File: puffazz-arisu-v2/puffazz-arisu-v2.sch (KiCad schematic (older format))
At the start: 185 parts, among them SW1 SW_Push, U1 ATmega32U4-AU, Y1 16MHz

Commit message: Finished scematic
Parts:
- removed D1: D_Schottky, symbol Device:D_Schottky
- added MX_#BKSP2: MX-NoLED, Button_Switch_Keyboard:SW_Cherry_MX_2.00u_PCB, symbol MX_Alps_Hybrid:MX-NoLED
- C1, C2, C3, C4, C5: footprint (none) -> Capacitor_SMD:C_0805_2012Metric
- C10, C11, C12, C13, C14, C15, C16, C17, C18, C19, C20, C21, C6, C7, C8, C9: renamed from C?; footprint (none) -> Capacitor_SMD:C_0805_2012Metric
- D10, D11, D12, D13, D14, D15, D16, D17, D18, D19, D2, D20, D21, D22, D23, D24, D25, D26, D27, D28, D29, D3, D30, D31, D32, D33, D34, D35, D36, D37, D38, D39, D4, D40, D41, D42, D43, D44, D45, D46, D47, D48, D49, D5, D50, D51, D52, D53, D54, D55, D56, D57, D58, D59, D6, D60, D61, D62, D63, D64, D65, D66, D67, D68, D7, D8, D9: renamed from D?; footprint (none) -> Diode_SMD:D_SOD-123
- F1: footprint (none) -> Fuse:Fuse_1206_3216Metric
- MX_"1, MX_#+1, MX_#-1, MX_#0, MX_#1, MX_#2, MX_#3, MX_#4, MX_#5, MX_#6, MX_#7, MX_#8, MX_#9, MX_#PGUP1, MX_#`1, MX_#|1, MX_:1, MX_<1, MX_>1, MX_?1, MX_A1, MX_B1, MX_C1, MX_D1, MX_DOWN1, MX_E1, MX_ESC1, MX_F1, MX_FN1, MX_G1, MX_H1, MX_I1, MX_J1, MX_K1, MX_L1, MX_LEFT1, MX_LWIN1, MX_M1, MX_N1, MX_O1, MX_P1, MX_PGDN1, MX_Q1, MX_R1, MX_RIGHT1, MX_S1, MX_T1, MX_U1, MX_UP1, MX_V1, MX_W1, MX_X1, MX_Y1, MX_Z1, MX_[1, MX_]1: footprint (none) -> Button_Switch_Keyboard:SW_Cherry_MX_1.00u_PCB
- MX_#TAB1, MX_LALT2, MX_LCTRL1, MX_RALT1: footprint (none) -> Button_Switch_Keyboard:SW_Cherry_MX_1.50u_PCB
- MX_BCKSP1, MX_SPACE1: footprint (none) -> Button_Switch_Keyboard:SW_Cherry_MX_2.00u_PCB
- MX_CAPS1, MX_CAPS2, MX_RSHIFT1: footprint (none) -> Button_Switch_Keyboard:SW_Cherry_MX_1.75u_PCB
- MX_LALT1: footprint (none) -> Button_Switch_Keyboard:SW_Cherry_MX_1.25u_PCB
- MX_LSHIFT1, MX_RETURN1, MX_SPACE2: footprint (none) -> Button_Switch_Keyboard:SW_Cherry_MX_2.25u_PCB
- MX_SPACE3: footprint (none) -> Button_Switch_Keyboard:SW_Cherry_MX_2.75u_PCB
- R1, R2, R3, R4, R5, R6: footprint (none) -> Resistor_SMD:R_0805_2012Metric
- SW1: footprint (none) -> Button_Switch_SMD:SW_SPST_SKQG_WithStem
- USB1: renamed from USB?; footprint (none) -> Connector_USB:USB_C_Receptacle_HRO_TYPE-C-31-M-12
- Y1: footprint (none) -> Crystal:Crystal_SMD_3225-4Pin_3.2x2.5mm
- gave numbers to parts that had none: 14
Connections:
- net labels added: ROW0, ROW1, ROW2, ROW3, ROW4, ROW5, ROW6, ROW7, ROW8, ROW9
- wire segments 251 -> 355
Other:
- moved on the sheet: D10, D11, D12, D13, D14, D15, D16, D17, D25, D26, D27, D28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

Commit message: Finished placing switch footprints on to the pcb
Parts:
- MX_BCKSP1: footprint Button_Switch_Keyboard:SW_Cherry_MX_2.00u_PCB -> Button_Switch_Keyboard:SW_Cherry_MX_1.50u_PCB
- MX_CAPS2: footprint Button_Switch_Keyboard:SW_Cherry_MX_1.75u_PCB -> Button_Switch_Keyboard:SW_Cherry_MX_1.00u_PCB
- U1: symbol MCU_Microchip_ATmega:ATmega32U4-AU -> puffazz-arisu-v2-rescue:ATmega32U4-AU-MCU_Microchip_ATmega
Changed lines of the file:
@@
 EESchema Schematic File Version 4
+LIBS:puffazz-arisu-v2-cache
 EELAYER 30 0
 EELAYER END
@@
 F 0 "MX_BCKSP1" H 13083 3223 60  0000 C CNN
 F 1 "MX-NoLED" H 13083 3149 20  0000 C CNN
-F 2 "Button_Switch_Keyboard:SW_Cherry_MX_2.00u_PCB" H 12425 2975 60  0001 C CNN
+F 2 "Button_Switch_Keyboard:SW_Cherry_MX_1.50u_PCB" H 12425 2975 60  0001 C CNN
 F 3 "" H 12425 2975 60  0001 C CNN
 	1    13050 3000
@@
 F 0 "MX_CAPS2" H 6033 4023 60  0000 C CNN
 F 1 "MX-NoLED" H 6033 3949 20  0000 C CNN
-F 2 "Button_Switch_Keyboard:SW_Cherry_MX_1.75u_PCB" H 5375 3775 60  0001 C CNN
+F 2 "Button_Switch_Keyboard:SW_Cherry_MX_1.00u_PCB" H 5375 3775 60  0001 C CNN
 F 3 "" H 5375 3775 60  0001 C CNN
 	1    6000 3800
@@
 	2900 4650 3350 4650
 $Comp
-L MCU_Microchip_ATmega:ATmega32U4-AU U1
+L puffazz-arisu-v2-rescue:ATmega32U4-AU-MCU_Microchip_ATmega U1
 U 1 1 5F269BC8
 P 2900 2850

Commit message: Fixed usb-c footprint not working with rats nest view
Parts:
- USB1: footprint Connector_USB:USB_C_Receptacle_HRO_TYPE-C-31-M-12 -> Type-C:HRO-TYPE-C-31-M-12-Assembly
- Y1: footprint Crystal:Crystal_SMD_3225-4Pin_3.2x2.5mm -> Type-C:HRO-TYPE-C-31-M-12-HandSoldering
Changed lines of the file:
@@
 F 0 "Y1" V 1854 1794 50  0000 L CNN
 F 1 "16MHz" V 1945 1794 50  0000 L CNN
-F 2 "Crystal:Crystal_SMD_3225-4Pin_3.2x2.5mm" H 1900 1650 50  0001 C CNN
+F 2 "Type-C:HRO-TYPE-C-31-M-12-HandSoldering" H 1900 1650 50  0001 C CNN
 F 3 "~" H 1900 1650 50  0001 C CNN
 	1    1900 1650
@@
 F 0 "USB1" H 1283 10447 60  0000 C CNN
 F 1 "HRO-TYPE-C-31-M-12" H 1283 10341 60  0000 C CNN
-F 2 "Connector_USB:USB_C_Receptacle_HRO_TYPE-C-31-M-12" H 1450 9650 60  0001 C CNN
+F 2 "Type-C:HRO-TYPE-C-31-M-12-Assembly" H 1450 9650 60  0001 C CNN
 F 3 "" H 1450 9650 60  0001 C CNN
 	1    1450 9650

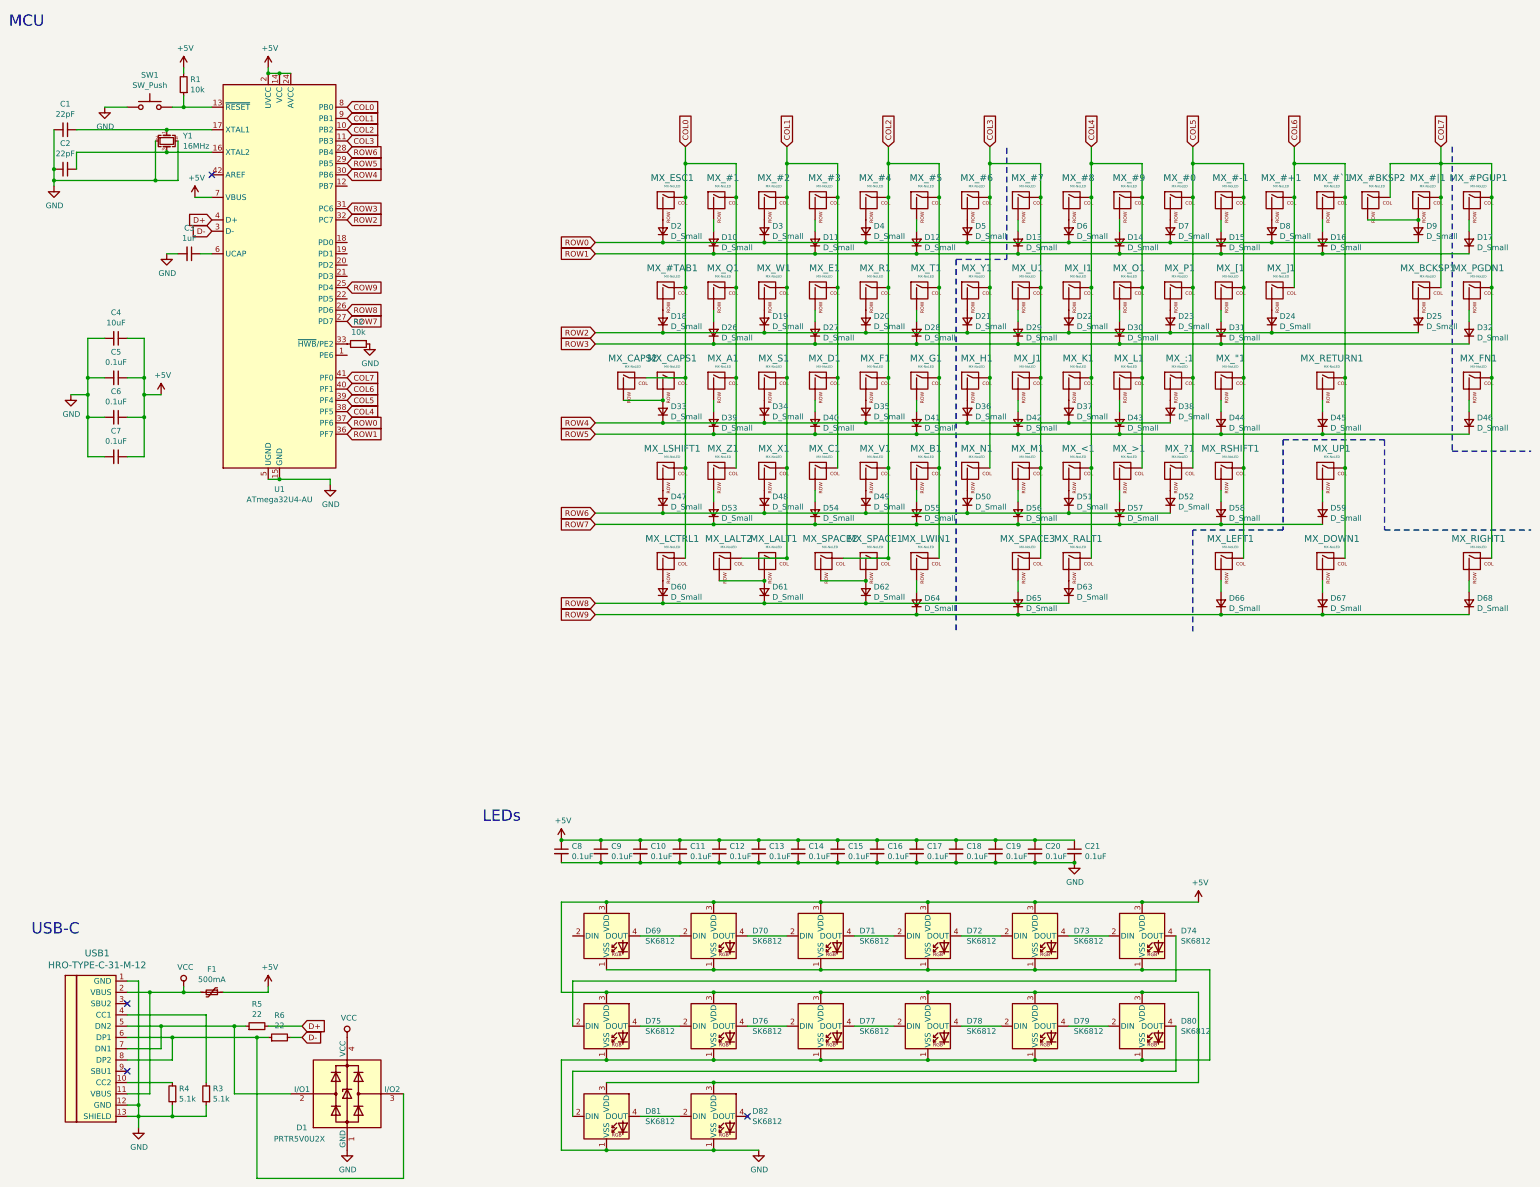
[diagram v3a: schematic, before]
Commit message: Finished routing switches and RGB LED
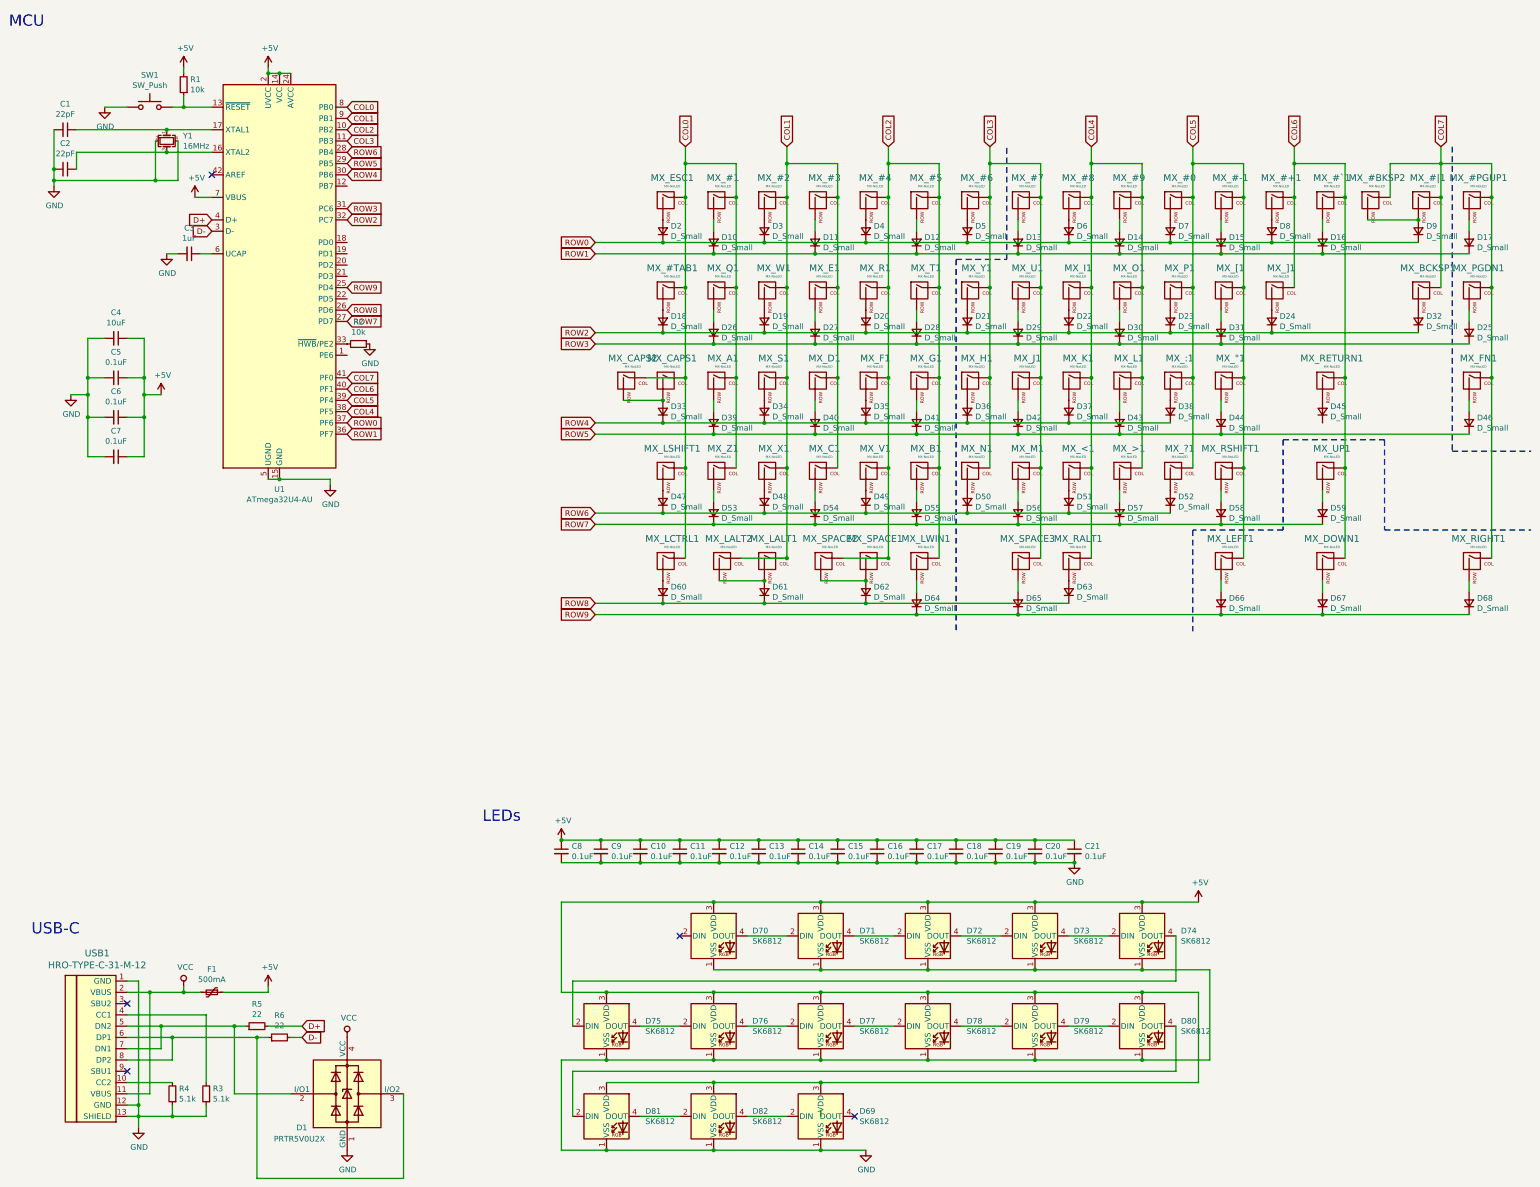
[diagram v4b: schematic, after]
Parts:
- Y1: footprint Type-C:HRO-TYPE-C-31-M-12-HandSoldering -> Crystal:Crystal_SMD_3225-4Pin_3.2x2.5mm_HandSoldering
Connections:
- net ROW2: now also D32.1 (K); no longer D25.1 (K)
- net ROW3: now also D25.1 (K); no longer D32.1 (K)
- net ROW5: no longer D45.1 (K)
- net at MX_BCKSP1.2 (ROW): now also D32.2 (A); no longer D25.2 (A)
- net at D69.2 (DIN): now also D82.4 (DOUT)
- net at D69.4 (DOUT): no longer D70.2 (DIN)
- net at MX_PGDN1.2 (ROW): now also D25.2 (A); no longer D32.2 (A)
- no-connect marks 4 -> 5
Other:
- moved on the sheet: D25, D32, D45, D69
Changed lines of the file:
@@
 F 0 "Y1" V 1854 1794 50  0000 L CNN
 F 1 "16MHz" V 1945 1794 50  0000 L CNN
-F 2 "Type-C:HRO-TYPE-C-31-M-12-HandSoldering" H 1900 1650 50  0001 C CNN
+F 2 "Crystal:Crystal_SMD_3225-4Pin_3.2x2.5mm_HandSoldering" H 1900 1650 50  0001 C CNN
 F 3 "~" H 1900 1650 50  0001 C CNN
 	1    1900 1650
@@
 $EndComp
 $Comp
-L Device:C_Small C4
-U 1 1 5F28E489
-P 1450 3400
-F 0 "C4" V 1221 3400 50  0000 C CNN
-F 1 "10uF" V 1312 3400 50  0000 C CNN
-F 2 "Capacitor_SMD:C_0805_2012Metric" H 1450 3400 50  0001 C CNN
-F 3 "~" H 1450 3400 50  0001 C CNN
-	1    1450 3400
-	0    1    1    0
-$EndComp
-$Comp
-L Device:C_Small C5
-U 1 1 5F28EF4D
-P 1450 3750
-F 0 "C5" V 1221 3750 50  0000 C CNN
-F 1 "0.1uF" V 1312 3750 50  0000 C CNN
-F 2 "Capacitor_SMD:C_0805_2012Metric" H 1450 3750 50  0001 C CNN
-F 3 "~" H 1450 3750 50  0001 C CNN
-	1    1450 3750
-	0    1    1    0
-$EndComp
-$Comp
-L Device:C_Small C6
-U 1 1 5F28F33C
-P 1450 4100
-F 0 "C6" V 1221 4100 50  0000 C CNN
-F 1 "0.1uF" V 1312 4100 50  0000 C CNN
-F 2 "Capacitor_SMD:C_0805_2012Metric" H 1450 4100 50  0001 C CNN
-F 3 "~" H 1450 4100 50  0001 C CNN
-	1    1450 4100
-	0    1    1    0
-$EndComp
-$Comp
-L Device:C_Small C7
-U 1 1 5F28F941
-P 1450 4450
-F 0 "C7" V 1221 4450 50  0000 C CNN
-F 1 "0.1uF" V 1312 4450 50  0000 C CNN
-F 2 "Capacitor_SMD:C_0805_2012Metric" H 1450 4450 50  0001 C CNN
-F 3 "~" H 1450 4450 50  0001 C CNN
-	1    1450 4450
-	0    1    1    0
-$EndComp
-Wire Wire Line
-	1350 3400 1200 3400
-Wire Wire Line
-	1200 3400 1200 3750
-Wire Wire Line
-	1200 4450 1350 4450
-Wire Wire Line
-	1350 4100 1200 4100
-Connection ~ 1200 4100
-Wire Wire Line
-	1200 4100 1200 4450
-Wire Wire Line
-	1350 3750 1200 3750
-Connection ~ 1200 3750
-Wire Wire Line
-	1200 3750 1200 3900
-Wire Wire Line
-	1550 3400 1700 3400
-Wire Wire Line
-	1700 4450 1550 4450
-Wire Wire Line
-	1550 4100 1700 4100
-Connection ~ 1700 4100
-Wire Wire Line
-	1700 4100 1700 4450
-Wire Wire Line
-	1550 3750 1700 3750
-Connection ~ 1700 3750
-Wire Wire Line
-	1700 3750 1700 3900
-Wire Wire Line
-	1700 3900 1850 3900
-Connection ~ 1700 3900
-Wire Wire Line
-	1700 3900 1700 4100
-$Comp
-L power:+5V #PWR0107
-U 1 1 5F296773
-P 1850 3900
-F 0 "#PWR0107" H 1850 3750 50  0001 C CNN
-F 1 "+5V" H 1865 4073 50  0000 C CNN
-F 2 "" H 1850 3900 50  0001 C CNN
-F 3 "" H 1850 3900 50  0001 C CNN
-	1    1850 3900
-	1    0    0    -1
-$EndComp
-$Comp
-L power:GND #PWR0108
-U 1 1 5F296B96
-P 1050 3900
-F 0 "#PWR0108" H 1050 3650 50  0001 C CNN
-F 1 "GND" H 1055 3727 50  0000 C CNN
-F 2 "" H 1050 3900 50  0001 C CNN
-F 3 "" H 1050 3900 50  0001 C CNN
-	1    1050 3900
-	1    0    0    -1
-$EndComp
-Wire Wire Line
-	1050 3900 1200 3900
-Connection ~ 1200 3900
-Wire Wire Line
-	1200 3900 1200 4100
-$Comp
 L Device:R_Small R2
 U 1 1 5F29845C
@@
 L LED:SK6812 D69
 U 1 1 5F3782C0
-P 5800 8700
-F 0 "D69" H 6144 8746 50  0000 L CNN
-F 1 "SK6812" H 6144 8655 50  0000 L CNN
-F 2 "LED_SMD:LED_SK6812_PLCC4_5.0x5.0mm_P3.2mm" H 5850 8400 50  0001 L TNN
-F 3 "https://cdn-shop.adafruit.com/product-files/1138/SK6812+LED+datasheet+.pdf" H 5900 8325 50  0001 L TNN
-	1    5800 8700
+P 7700 10300
+F 0 "D69" H 8044 10346 50  0000 L CNN
+F 1 "SK6812" H 8044 10255 50  0000 L CNN
+F 2 "LED_SMD:LED_SK6812_PLCC4_5.0x5.0mm_P3.2mm" H 7750 10000 50  0001 L TNN
+F 3 "https://cdn-shop.adafruit.com/product-files/1138/SK6812+LED+datasheet+.pdf" H 7800 9925 50  0001 L TNN
+	1    7700 10300
 	1    0    0    -1
 $EndComp
@@
 $EndComp
 Wire Wire Line
-	6100 8700 6450 8700
-Wire Wire Line
 	7050 8700 7400 8700
 Wire Wire Line
@@
 Wire Wire Line
 	6100 10300 6450 10300
-NoConn ~ 7050 10300
 $Comp
 L power:+5V #PWR0115
@@
 	11050 8400 10550 8400
 Connection ~ 6750 8400
-Wire Wire Line
-	6750 8400 5800 8400
 Connection ~ 7700 8400
 Wire Wire Line
@@
 	10550 8400 9600 8400
 Wire Wire Line
-	5800 8400 5400 8400
-Wire Wire Line
 	5400 8400 5400 9200
 Wire Wire Line
 	5400 9200 5800 9200
-Connection ~ 5800 8400
 Connection ~ 5800 9200
 Wire Wire Line
@@
 	11050 9200 11050 10000
 Wire Wire Line
-	11050 10000 6750 10000
+	11050 10000 7700 10000
 Connection ~ 10550 9200
 Connection ~ 6750 10000
@@
 	6750 10000 5800 10000
 Wire Wire Line
-	5800 9000 6750 9000
-Wire Wire Line
 	11150 9000 11150 9800
 Wire Wire Line
 	11150 9800 10550 9800
-Connection ~ 6750 9000
 Wire Wire Line
 	6750 9000 7700 9000
@@
 L power:GND #PWR0116
 U 1 1 5F400838
-P 7150 10600
-F 0 "#PWR0116" H 7150 10350 50  0001 C CNN
-F 1 "GND" H 7155 10427 50  0000 C CNN
-F 2 "" H 7150 10600 50  0001 C CNN
-F 3 "" H 7150 10600 50  0001 C CNN
-	1    7150 10600
+P 8100 10600
+F 0 "#PWR0116" H 8100 10350 50  0001 C CNN
+F 1 "GND" H 8105 10427 50  0000 C CNN
+F 2 "" H 8100 10600 50  0001 C CNN
+F 3 "" H 8100 10600 50  0001 C CNN
+	1    8100 10600
 	1    0    0    -1
 $EndComp
-Wire Wire Line
-	7150 10600 6750 10600
 Connection ~ 6750 10600
 Text Notes 4700 7700 0    100  ~ 0
@@
 L Device:D_Small D25
 U 1 1 5F3E1B60
-P 13000 3250
-F 0 "D25" V 13046 3180 50  0000 R CNN
-F 1 "D_Small" V 12955 3180 50  0000 R CNN
-F 2 "Diode_SMD:D_SOD-123" V 13000 3250 50  0001 C CNN
-F 3 "~" V 13000 3250 50  0001 C CNN
-	1    13000 3250
+P 13450 3350
+F 0 "D25" V 13496 3280 50  0000 R CNN
+F 1 "D_Small" V 13405 3280 50  0000 R CNN
+F 2 "Diode_SMD:D_SOD-123" V 13450 3350 50  0001 C CNN
+F 3 "~" V 13450 3350 50  0001 C CNN
+	1    13450 3350
 	0    -1   -1   0
 $EndComp
@@
 L Device:D_Small D32
 U 1 1 5F4270C8
-P 13450 3350
-F 0 "D32" V 13496 3280 50  0000 R CNN
-F 1 "D_Small" V 13405 3280 50  0000 R CNN
-F 2 "Diode_SMD:D_SOD-123" V 13450 3350 50  0001 C CNN
-F 3 "~" V 13450 3350 50  0001 C CNN
-	1    13450 3350
+P 13000 3250
+F 0 "D32" V 13046 3180 50  0000 R CNN
+F 1 "D_Small" V 12955 3180 50  0000 R CNN
+F 2 "Diode_SMD:D_SOD-123" V 13000 3250 50  0001 C CNN
+F 3 "~" V 13000 3250 50  0001 C CNN
+	1    13000 3250
 	0    -1   -1   0
 $EndComp
@@
 L Device:D_Small D45
 U 1 1 5F4541F9
-P 12150 4150
-F 0 "D45" V 12196 4080 50  0000 R CNN
-F 1 "D_Small" V 12105 4080 50  0000 R CNN
-F 2 "Diode_SMD:D_SOD-123" V 12150 4150 50  0001 C CNN
-F 3 "~" V 12150 4150 50  0001 C CNN
-	1    12150 4150
+P 12150 4050
+F 0 "D45" V 12196 3980 50  0000 R CNN
+F 1 "D_Small" V 12105 3980 50  0000 R CNN
+F 2 "Diode_SMD:D_SOD-123" V 12150 4050 50  0001 C CNN
+F 3 "~" V 12150 4050 50  0001 C CNN
+	1    12150 4050
 	0    -1   -1   0
 $EndComp
@@
 	11250 4050 11250 3950
 Wire Wire Line
-	12150 4050 12150 3950
-Wire Wire Line
 	13450 4050 13450 3950
 Wire Wire Line
@@
 	10350 4250 11250 4250
 Connection ~ 11250 4250
-Wire Wire Line
-	11250 4250 12150 4250
 Text GLabel 5700 4150 0    50   Input ~ 0
 ROW4
@@
 Connection ~ 11250 3450
 Wire Wire Line
-	12150 4250 13450 4250
-Connection ~ 12150 4250
-Wire Wire Line
 	12150 5850 13450 5850
 Connection ~ 12150 5850
@@
 Wire Wire Line
 	2800 1050 2900 1050
-Wire Wire Line
-	1700 3400 1700 3750
 Connection ~ 2900 4650
 Wire Wire Line
@@
 	12550 2350 13000 2350
 Connection ~ 13000 2350
+Wire Wire Line
+	1700 3400 1700 3750
+Wire Wire Line
+	1200 3900 1200 4100
+Connection ~ 1200 3900
+Wire Wire Line
+	1050 3900 1200 3900
+$Comp
+L power:GND #PWR0108
+U 1 1 5F296B96
+P 1050 3900
+F 0 "#PWR0108" H 1050 3650 50  0001 C CNN
+F 1 "GND" H 1055 3727 50  0000 C CNN
+F 2 "" H 1050 3900 50  0001 C CNN
+F 3 "" H 1050 3900 50  0001 C CNN
+	1    1050 3900
+	1    0    0    -1
+$EndComp
+$Comp
+L power:+5V #PWR0107
+U 1 1 5F296773
+P 1850 3900
+F 0 "#PWR0107" H 1850 3750 50  0001 C CNN
+F 1 "+5V" H 1865 4073 50  0000 C CNN
+F 2 "" H 1850 3900 50  0001 C CNN
+F 3 "" H 1850 3900 50  0001 C CNN
+	1    1850 3900
+	1    0    0    -1
+$EndComp
+Wire Wire Line
+	1700 3900 1700 4100
+Connection ~ 1700 3900
+Wire Wire Line
+	1700 3900 1850 3900
+Wire Wire Line
+	1700 3750 1700 3900
+Connection ~ 1700 3750
+Wire Wire Line
+	1550 3750 1700 3750
+Wire Wire Line
+	1700 4100 1700 4450
+Connection ~ 1700 4100
+Wire Wire Line
+	1550 4100 1700 4100
+Wire Wire Line
+	1700 4450 1550 4450
+Wire Wire Line
+	1550 3400 1700 3400
+Wire Wire Line
+	1200 3750 1200 3900
+Connection ~ 1200 3750
+Wire Wire Line
+	1350 3750 1200 3750
+Wire Wire Line
+	1200 4100 1200 4450
+Connection ~ 1200 4100
+Wire Wire Line
+	1350 4100 1200 4100
+Wire Wire Line
+	1200 4450 1350 4450
+Wire Wire Line
+	1200 3400 1200 3750
+Wire Wire Line
+	1350 3400 1200 3400
+$Comp
+L Device:C_Small C7
+U 1 1 5F28F941
+P 1450 4450
+F 0 "C7" V 1221 4450 50  0000 C CNN
+F 1 "0.1uF" V 1312 4450 50  0000 C CNN
+F 2 "Capacitor_SMD:C_0805_2012Metric" H 1450 4450 50  0001 C CNN
+F 3 "~" H 1450 4450 50  0001 C CNN
+	1    1450 4450
+	0    1    1    0
+$EndComp
+$Comp
+L Device:C_Small C6
+U 1 1 5F28F33C
+P 1450 4100
+F 0 "C6" V 1221 4100 50  0000 C CNN
+F 1 "0.1uF" V 1312 4100 50  0000 C CNN
+F 2 "Capacitor_SMD:C_0805_2012Metric" H 1450 4100 50  0001 C CNN
+F 3 "~" H 1450 4100 50  0001 C CNN
+	1    1450 4100
+	0    1    1    0
+$EndComp
+$Comp
+L Device:C_Small C5
+U 1 1 5F28EF4D
+P 1450 3750
+F 0 "C5" V 1221 3750 50  0000 C CNN
+F 1 "0.1uF" V 1312 3750 50  0000 C CNN
+F 2 "Capacitor_SMD:C_0805_2012Metric" H 1450 3750 50  0001 C CNN
+F 3 "~" H 1450 3750 50  0001 C CNN
+	1    1450 3750
+	0    1    1    0
+$EndComp
+$Comp
+L Device:C_Small C4
+U 1 1 5F28E489
+P 1450 3400
+F 0 "C4" V 1221 3400 50  0000 C CNN
+F 1 "10uF" V 1312 3400 50  0000 C CNN
+F 2 "Capacitor_SMD:C_0805_2012Metric" H 1450 3400 50  0001 C CNN
+F 3 "~" H 1450 3400 50  0001 C CNN
+	1    1450 3400
+	0    1    1    0
+$EndComp
+Wire Wire Line
+	11250 4250 13450 4250
+Wire Wire Line
+	7700 10300 7700 10250
+Connection ~ 7700 10000
+Wire Wire Line
+	7700 10000 6750 10000
+Wire Wire Line
+	5400 8400 6750 8400
+Wire Wire Line
+	6750 10600 7700 10600
+Connection ~ 7700 10600
+Wire Wire Line
+	7700 10600 8100 10600
+Wire Wire Line
+	7400 10300 7050 10300
+NoConn ~ 8000 10300
+NoConn ~ 6450 8700
 $EndSCHEMATC
